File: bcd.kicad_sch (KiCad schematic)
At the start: 0 parts

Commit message: added decoupling caps
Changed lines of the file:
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@@
 	(paper "A4")
 	(junction
+		(at 55.88 99.06)
+		(diameter 0)
+		(color 0 0 0 0)
+	)
+	(junction
 		(at 121.92 113.03)
 		(diameter 0)
@@
 	)
 	(junction
-		(at 55.88 99.06)
-		(diameter 0)
-		(color 0 0 0 0)
-	)
-	(junction
 		(at 208.28 91.44)
 		(diameter 0)
@@
 	)
 	(symbol
-		(lib_id "power:VDD")
+		(lib_id "power:+3V3")
 		(at 55.88 99.06 0)
 		(unit 1)
@@
 			)
 		)
-		(property "Value" "VDD"
+		(property "Value" "+3V3"
 			(at 55.88 94.9269 0)
 			(effects
@@
 			)
 		)
-		(property "Description" "Power symbol creates a global label with name \"VDD\""
+		(property "Description" "Power symbol creates a global label with name \"+3V3\""
 			(at 55.88 99.06 0)
 			(effects

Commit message: schematic cleanup, routed 1 bdc
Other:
- sheet NAND2: file and.kicad_sch -> nand.kicad_sch
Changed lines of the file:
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@@
 		(dnp no)
 		(fields_autoplaced yes)
-		(property "Reference" "#PWR0130"
+		(property "Reference" "#PWR042"
 			(at 55.88 102.87 0)
 			(effects
@@
 			(project "transistor-clock"
 				(path "/ce10d5bc-995e-4952-aa76-0a08f713a0f2/2c36a9e9-de42-4705-9ad4-94f4cc168e2f/213ead95-e2da-4b6f-a756-d929eb6dfb1c"
-					(reference "#PWR0320")
+					(reference "#PWR0252")
 					(unit 1)
 				)
 				(path "/ce10d5bc-995e-4952-aa76-0a08f713a0f2/2c36a9e9-de42-4705-9ad4-94f4cc168e2f/230aee3b-3cdc-400c-8fed-9199df89dadd"
-					(reference "#PWR0130")
+					(reference "#PWR042")
 					(unit 1)
 				)
 				(path "/ce10d5bc-995e-4952-aa76-0a08f713a0f2/2c36a9e9-de42-4705-9ad4-94f4cc168e2f/6fa12e35-b957-4335-be8e-d0857c2dd0bf"
-					(reference "#PWR0196")
+					(reference "#PWR0224")
 					(unit 1)
 				)
@@
 			)
 		)
-		(property "Sheetfile" "and.kicad_sch"
+		(property "Sheetfile" "nand.kicad_sch"
 			(at 185.42 97.1046 0)
 			(effects

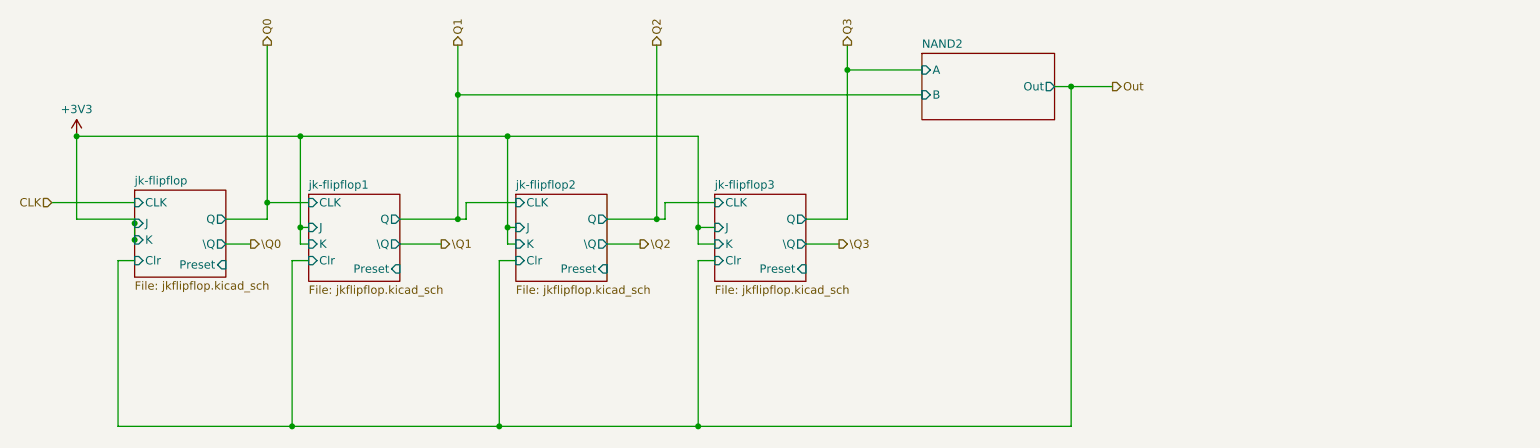
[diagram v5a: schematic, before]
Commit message: switched to using flipflop module
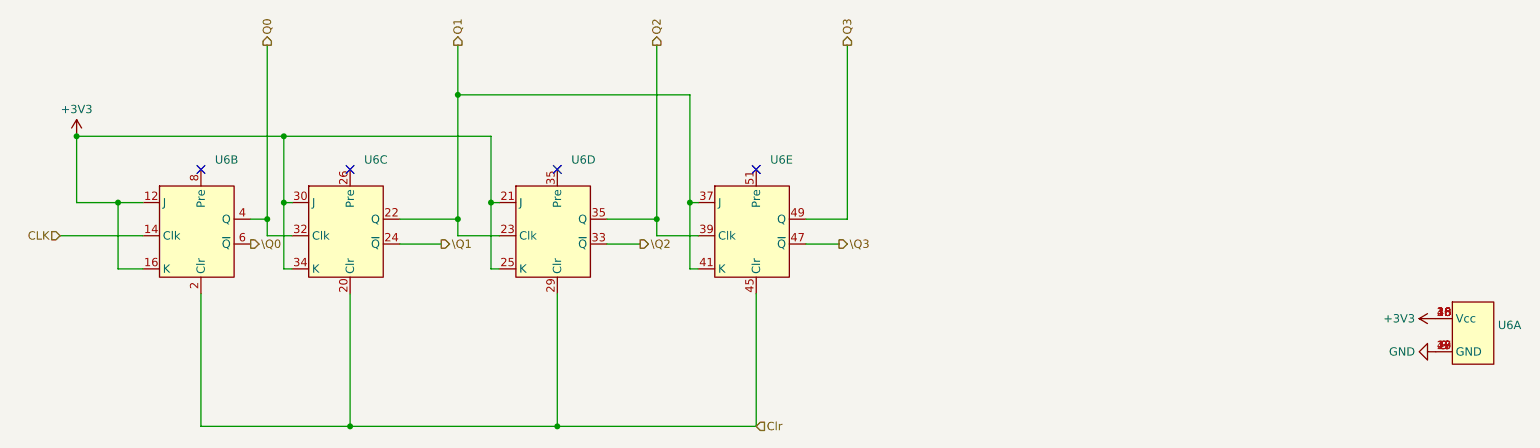
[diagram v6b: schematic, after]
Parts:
- added U6: ~, symbol custom:jk-flipflops
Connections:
- net +3V3: now also U6.10 (Vcc), U6.12 (J), U6.16 (K), U6.18 (Vcc), U6.21 (J), U6.25 (K), U6.28 (Vcc), U6.30 (J), U6.34 (K), U6.36 (Vcc), U6.46 (Vcc)
- net CLK: now also U6.14 (Clk)
- net Q0: now also U6.32 (Clk), U6.4 (Q)
- net Q1: now also U6.22 (Q), U6.23 (Clk), U6.37 (J), U6.41 (K)
- net Q2: now also U6.35 (Q), U6.39 (Clk)
- net Q3: now also U6.49 (Q)
- net \Q0: now also U6.6 (~{Q})
- net \Q1: now also U6.24 (~{Q})
- net \Q2: now also U6.33 (~{Q})
- net \Q3: now also U6.47 (~{Q})
- new net Clr: U6.2 (Clr), U6.20 (Clr), U6.29 (Clr), U6.45 (Clr)
- new net GND: U6.19 (GND), U6.27 (GND), U6.3 (GND), U6.43 (GND), U6.9 (GND)
- no-connect marks 0 -> 4
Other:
- removed sheet NAND2
- removed sheet jk-flipflop
- removed sheet jk-flipflop1
- removed sheet jk-flipflop2
- removed sheet jk-flipflop3

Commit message: switched to using SSR module
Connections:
- net +3V3: no longer U6.10 (Vcc), U6.12 (J), U6.16 (K), U6.18 (Vcc), U6.21 (J), U6.25 (K), U6.28 (Vcc), U6.30 (J), U6.34 (K), U6.36 (Vcc), U6.46 (Vcc)
- net CLK: no longer U6.14 (Clk)
- net Clr: no longer U6.2 (Clr), U6.20 (Clr), U6.29 (Clr), U6.45 (Clr)
- net GND: no longer U6.19 (GND), U6.27 (GND), U6.3 (GND), U6.43 (GND), U6.9 (GND)
- net Q0: no longer U6.32 (Clk), U6.4 (Q)
- net Q2: no longer U6.35 (Q), U6.39 (Clk)
- net Q3: no longer U6.49 (Q)
- net \Q0: no longer U6.6 (~{Q})
- net \Q1: no longer U6.24 (~{Q})
- net \Q2: no longer U6.33 (~{Q})
- net \Q3: no longer U6.47 (~{Q})
- removed net Q1: U6.22 (Q), U6.23 (Clk), U6.37 (J), U6.41 (K)
- new net Gnd: U6.19 (Gnd), U6.27 (Gnd), U6.3 (Gnd), U6.43 (Gnd), U6.9 (Gnd)
- new net Vcc: U6.10 (Vcc), U6.18 (Vcc), U6.28 (Vcc), U6.36 (Vcc), U6.46 (Vcc)
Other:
- moved on the sheet: U6B, U6C, U6D
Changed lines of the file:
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@@
 	)
 	(symbol
-		(lib_name "jk-flipflops_2")
 		(lib_id "custom:jk-flipflops")
 		(at 85.09 102.87 0)
@@
 		)
 		(instances
-			(project ""
+			(project "transistor-clock"
 				(path "/ce10d5bc-995e-4952-aa76-0a08f713a0f2/2c36a9e9-de42-4705-9ad4-94f4cc168e2f/213ead95-e2da-4b6f-a756-d929eb6dfb1c"
 					(reference "U8")
@@
 		)
 		(instances
-			(project ""
+			(project "transistor-clock"
 				(path "/ce10d5bc-995e-4952-aa76-0a08f713a0f2/2c36a9e9-de42-4705-9ad4-94f4cc168e2f/213ead95-e2da-4b6f-a756-d929eb6dfb1c"
 					(reference "#PWR022")
@@
 	)
 	(symbol
-		(lib_name "jk-flipflops_4")
+		(lib_name "jk-flipflops_2")
 		(lib_id "custom:jk-flipflops")
 		(at 147.32 102.87 0)
@@
 		)
 		(instances
-			(project ""
+			(project "transistor-clock"
 				(path "/ce10d5bc-995e-4952-aa76-0a08f713a0f2/2c36a9e9-de42-4705-9ad4-94f4cc168e2f/213ead95-e2da-4b6f-a756-d929eb6dfb1c"
 					(reference "U8")
@@
 	)
 	(symbol
-		(lib_name "jk-flipflops_3")
+		(lib_name "jk-flipflops_4")
 		(lib_id "custom:jk-flipflops")
 		(at 116.84 104.14 0)
@@
 		)
 		(instances
-			(project ""
+			(project "transistor-clock"
 				(path "/ce10d5bc-995e-4952-aa76-0a08f713a0f2/2c36a9e9-de42-4705-9ad4-94f4cc168e2f/213ead95-e2da-4b6f-a756-d929eb6dfb1c"
 					(reference "U8")
@@
 	)
 	(symbol
+		(lib_name "jk-flipflops_1")
 		(lib_id "custom:jk-flipflops")
 		(at 259.08 124.46 0)
@@
 		)
 		(instances
-			(project ""
+			(project "transistor-clock"
 				(path "/ce10d5bc-995e-4952-aa76-0a08f713a0f2/2c36a9e9-de42-4705-9ad4-94f4cc168e2f/213ead95-e2da-4b6f-a756-d929eb6dfb1c"
 					(reference "U8")
@@
 	)
 	(symbol
-		(lib_name "jk-flipflops_1")
+		(lib_name "jk-flipflops_3")
 		(lib_id "custom:jk-flipflops")
 		(at 64.77 105.41 0)
@@
 		)
 		(instances
-			(project ""
+			(project "transistor-clock"
 				(path "/ce10d5bc-995e-4952-aa76-0a08f713a0f2/2c36a9e9-de42-4705-9ad4-94f4cc168e2f/213ead95-e2da-4b6f-a756-d929eb6dfb1c"
 					(reference "U8")
